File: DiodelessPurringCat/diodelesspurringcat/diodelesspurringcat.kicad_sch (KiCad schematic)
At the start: 21 parts, among them J1 ScreenL, U1 ProMicro-kbd

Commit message: trying to make a reversible nice view
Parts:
- 0/9, 1/8, 10/19, 11/18, 12/17, 13/16, 14/15, 2/7, 20/25, 21/24, 22/23, 26/29, 27/28, 3/6, 4/5: footprint keyswitches:Kailh_socket_PG1350_reversible -> chelming-kbd:choc_v1_hotswap_reversible_no_extras
- J1: value ScreenL -> nice!view; footprint Connector_PinHeader_2.54mm:PinHeader_1x05_P2.54mm_Vertical -> chelming-kbd:nice-view_reversible
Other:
- moved on the sheet: J1
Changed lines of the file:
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@@
 	(polyline
 		(pts
-			(xy 227.33 124.46) (xy 205.74 124.46)
+			(xy 199.39 118.11) (xy 199.39 96.52)
 		)
 		(stroke
@@
 		)
 	)
+	(wire
+		(pts
+			(xy 205.74 111.76) (xy 208.28 111.76)
+		)
+		(stroke
+			(width 0)
+			(type default)
+		)
+	)
+	(wire
+		(pts
+			(xy 207.01 104.14) (xy 215.9 104.14)
+		)
+		(stroke
+			(width 0)
+			(type default)
+		)
+	)
+	(wire
+		(pts
+			(xy 205.74 116.84) (xy 215.9 116.84)
+		)
+		(stroke
+			(width 0)
+			(type default)
+		)
+	)
+	(wire
+		(pts
+			(xy 215.9 97.79) (xy 215.9 101.6)
+		)
+		(stroke
+			(width 0)
+			(type default)
+		)
+	)
+	(wire
+		(pts
+			(xy 215.9 116.84) (xy 215.9 111.76)
+		)
+		(stroke
+			(width 0)
+			(type default)
+		)
+	)
 	(polyline
 		(pts
-			(xy 227.33 90.17) (xy 227.33 124.46)
+			(xy 233.68 118.11) (xy 199.39 118.11)
 		)
 		(stroke
@@
 	(polyline
 		(pts
-			(xy 205.74 124.46) (xy 205.74 90.17)
+			(xy 199.39 96.52) (xy 233.68 96.52)
 		)
 		(stroke
@@
 	(polyline
 		(pts
-			(xy 205.74 90.17) (xy 227.33 90.17)
+			(xy 233.68 96.52) (xy 233.68 118.11)
 		)
 		(stroke
@@
 		)
 	)
+	(wire
+		(pts
+			(xy 208.28 109.22) (xy 215.9 109.22)
+		)
+		(stroke
+			(width 0)
+			(type default)
+		)
+	)
+	(wire
+		(pts
+			(xy 207.01 106.68) (xy 215.9 106.68)
+		)
+		(stroke
+			(width 0)
+			(type default)
+		)
+	)
+	(wire
+		(pts
+			(xy 208.28 111.76) (xy 208.28 109.22)
+		)
+		(stroke
+			(width 0)
+			(type default)
+		)
+	)
 	(polyline
 		(pts
@@
 		)
 	)
+	(wire
+		(pts
+			(xy 207.01 97.79) (xy 215.9 97.79)
+		)
+		(stroke
+			(width 0)
+			(type default)
+		)
+	)
 	(polyline
 		(pts
@@
 	(text "Screen"
 		(exclude_from_sim no)
-		(at 207.01 95.25 0)
+		(at 199.136 95.25 0)
 		(effects
 			(font
@@
 	(global_label "gnd"
 		(shape input)
-		(at 218.44 109.22 270)
-		(fields_autoplaced yes)
-		(effects
-			(font
-				(size 1.27 1.27)
-			)
-			(justify right)
-		)
-		(property "Intersheetrefs" "${INTERSHEET_REFS}"
-			(at 218.3606 114.9913 90)
+		(at 205.74 111.76 180)
+		(fields_autoplaced yes)
+		(effects
+			(font
+				(size 1.27 1.27)
+			)
+			(justify right)
+		)
+		(property "Intersheetrefs" "${INTERSHEET_REFS}"
+			(at 199.962 111.76 0)
 			(effects
 				(font
@@
 	(global_label "CS"
 		(shape input)
-		(at 220.98 109.22 270)
-		(fields_autoplaced yes)
-		(effects
-			(font
-				(size 1.27 1.27)
-			)
-			(justify right)
-		)
-		(property "Intersheetrefs" "${INTERSHEET_REFS}"
-			(at 220.9006 114.0237 90)
+		(at 205.74 116.84 180)
+		(fields_autoplaced yes)
+		(effects
+			(font
+				(size 1.27 1.27)
+			)
+			(justify right)
+		)
+		(property "Intersheetrefs" "${INTERSHEET_REFS}"
+			(at 200.9295 116.84 0)
 			(effects
 				(font
@@
 	(global_label "vcc"
 		(shape input)
-		(at 215.9 109.22 270)
-		(fields_autoplaced yes)
-		(effects
-			(font
-				(size 1.27 1.27)
-			)
-			(justify right)
-		)
-		(property "Intersheetrefs" "${INTERSHEET_REFS}"
-			(at 215.8206 114.689 90)
+		(at 207.01 106.68 180)
+		(fields_autoplaced yes)
+		(effects
+			(font
+				(size 1.27 1.27)
+			)
+			(justify right)
+		)
+		(property "Intersheetrefs" "${INTERSHEET_REFS}"
+			(at 201.5342 106.68 0)
 			(effects
 				(font
@@
 	(global_label "SCK"
 		(shape input)
-		(at 213.36 109.22 270)
-		(fields_autoplaced yes)
-		(effects
-			(font
-				(size 1.27 1.27)
-			)
-			(justify right)
-		)
-		(property "Intersheetrefs" "${INTERSHEET_REFS}"
-			(at 213.2806 115.2937 90)
+		(at 207.01 104.14 180)
+		(fields_autoplaced yes)
+		(effects
+			(font
+				(size 1.27 1.27)
+			)
+			(justify right)
+		)
+		(property "Intersheetrefs" "${INTERSHEET_REFS}"
+			(at 200.9295 104.14 0)
 			(effects
 				(font
@@
 	(global_label "MOSI"
 		(shape input)
-		(at 210.82 109.22 270)
-		(fields_autoplaced yes)
-		(effects
-			(font
-				(size 1.27 1.27)
-			)
-			(justify right)
-		)
-		(property "Intersheetrefs" "${INTERSHEET_REFS}"
-			(at 210.7406 116.1404 90)
+		(at 207.01 97.79 180)
+		(fields_autoplaced yes)
+		(effects
+			(font
+				(size 1.27 1.27)
+			)
+			(justify right)
+		)
+		(property "Intersheetrefs" "${INTERSHEET_REFS}"
+			(at 200.0828 97.79 0)
 			(effects
 				(font
@@
 			)
 		)
-		(property "Footprint" "keyswitches:Kailh_socket_PG1350_reversible"
+		(property "Footprint" "chelming-kbd:choc_v1_hotswap_reversible_no_extras"
 			(at 26.67 33.02 0)
 			(effects
@@
 			)
 		)
-		(property "Footprint" "keyswitches:Kailh_socket_PG1350_reversible"
+		(property "Footprint" "chelming-kbd:choc_v1_hotswap_reversible_no_extras"
 			(at 49.53 24.13 0)
 			(effects
@@
 			)
 		)
-		(property "Footprint" "keyswitches:Kailh_socket_PG1350_reversible"
+		(property "Footprint" "chelming-kbd:choc_v1_hotswap_reversible_no_extras"
 			(at 72.39 20.32 0)
 			(effects
@@
 			)
 		)
-		(property "Footprint" "keyswitches:Kailh_socket_PG1350_reversible"
+		(property "Footprint" "chelming-kbd:choc_v1_hotswap_reversible_no_extras"
 			(at 95.25 24.13 0)
 			(effects
@@
 			)
 		)
-		(property "Footprint" "keyswitches:Kailh_socket_PG1350_reversible"
+		(property "Footprint" "chelming-kbd:choc_v1_hotswap_reversible_no_extras"
 			(at 95.25 86.36 0)
 			(effects
@@
 			)
 		)
-		(property "Footprint" "keyswitches:Kailh_socket_PG1350_reversible"
+		(property "Footprint" "chelming-kbd:choc_v1_hotswap_reversible_no_extras"
 			(at 26.67 54.61 0)
 			(effects
@@
 			)
 		)
-		(property "Footprint" "keyswitches:Kailh_socket_PG1350_reversible"
+		(property "Footprint" "chelming-kbd:choc_v1_hotswap_reversible_no_extras"
 			(at 49.53 45.72 0)
 			(effects
@@
 			)
 		)
-		(property "Footprint" "keyswitches:Kailh_socket_PG1350_reversible"
+		(property "Footprint" "chelming-kbd:choc_v1_hotswap_reversible_no_extras"
 			(at 72.39 41.91 0)
 			(effects
@@
 			)
 		)
-		(property "Footprint" "keyswitches:Kailh_socket_PG1350_reversible"
+		(property "Footprint" "chelming-kbd:choc_v1_hotswap_reversible_no_extras"
 			(at 95.25 45.72 0)
 			(effects
@@
 			)
 		)
-		(property "Footprint" "keyswitches:Kailh_socket_PG1350_reversible"
+		(property "Footprint" "chelming-kbd:choc_v1_hotswap_reversible_no_extras"
 			(at 49.53 64.77 0)
 			(effects
@@
 			)
 		)
-		(property "Footprint" "keyswitches:Kailh_socket_PG1350_reversible"
+		(property "Footprint" "chelming-kbd:choc_v1_hotswap_reversible_no_extras"
 			(at 72.39 60.96 0)
 			(effects
@@
 			)
 		)
-		(property "Footprint" "keyswitches:Kailh_socket_PG1350_reversible"
+		(property "Footprint" "chelming-kbd:choc_v1_hotswap_reversible_no_extras"
 			(at 95.25 64.77 0)
 			(effects
@@
 			)
 		)
-		(property "Footprint" "keyswitches:Kailh_socket_PG1350_reversible"
+		(property "Footprint" "chelming-kbd:choc_v1_hotswap_reversible_no_extras"
 			(at 118.11 34.29 0)
 			(effects
@@
 			)
 		)
-		(property "Footprint" "keyswitches:Kailh_socket_PG1350_reversible"
+		(property "Footprint" "chelming-kbd:choc_v1_hotswap_reversible_no_extras"
 			(at 118.11 55.88 0)
 			(effects
@@
 	(symbol
 		(lib_id "Connector_Generic:Conn_01x05")
-		(at 215.9 104.14 90)
+		(at 220.98 106.68 0)
 		(unit 1)
 		(exclude_from_sim no)
@@
 		(fields_autoplaced yes)
 		(property "Reference" "J1"
-			(at 215.9 97.79 90)
-			(effects
-				(font
-					(size 1.27 1.27)
-				)
-			)
-		)
-		(property "Value" "ScreenL"
-			(at 215.9 100.33 90)
-			(effects
-				(font
-					(size 1.27 1.27)
-				)
-			)
-		)
-		(property "Footprint" "Connector_PinHeader_2.54mm:PinHeader_1x05_P2.54mm_Vertical"
-			(at 215.9 104.14 0)
+			(at 227.33 106.68 90)
+			(effects
+				(font
+					(size 1.27 1.27)
+				)
+			)
+		)
+		(property "Value" "nice!view"
+			(at 224.79 106.68 90)
+			(effects
+				(font
+					(size 1.27 1.27)
+				)
+			)
+		)
+		(property "Footprint" "chelming-kbd:nice-view_reversible"
+			(at 220.98 106.68 0)
 			(effects
 				(font
@@
 		)
 		(property "Datasheet" "~"
-			(at 215.9 104.14 0)
+			(at 220.98 106.68 0)
 			(effects
 				(font
@@
 		)
 		(property "Description" ""
-			(at 215.9 104.14 0)
+			(at 220.98 106.68 0)
 			(effects
 				(font
@@
 			)
 		)
-		(property "Footprint" "keyswitches:Kailh_socket_PG1350_reversible"
+		(property "Footprint" "chelming-kbd:choc_v1_hotswap_reversible_no_extras"
 			(at 118.11 86.36 0)
 			(effects

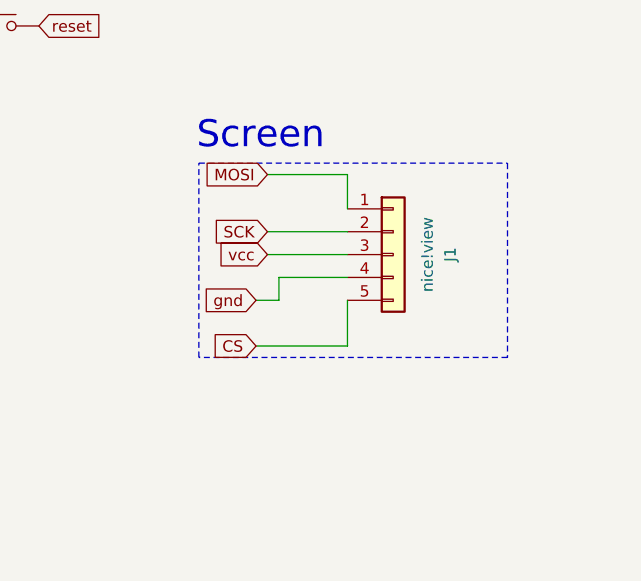
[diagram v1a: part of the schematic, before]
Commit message: moving back to reversible. still diodeless. needs case mounts
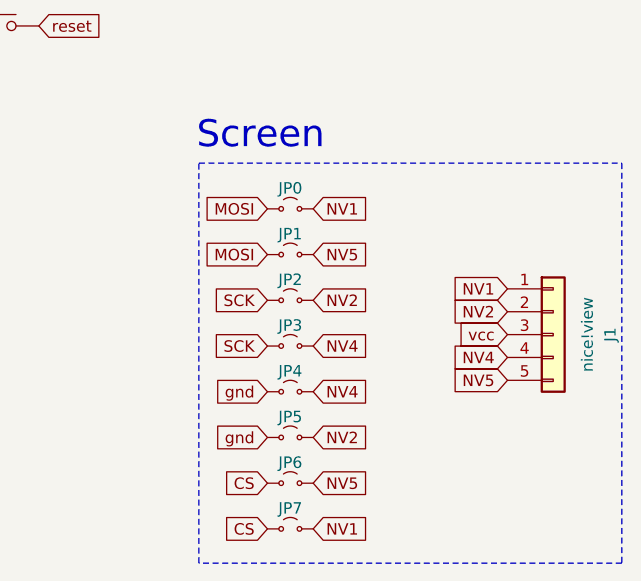
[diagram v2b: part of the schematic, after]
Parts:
- added JP0, JP1, JP2, JP3, JP4, JP5, JP6, JP7: Jumper_2_Small_Open, Jumper:SolderJumper-2_P1.3mm_Open_TrianglePad1.0x1.5mm, symbol Jumper:Jumper_2_Small_Open
- J1: footprint chelming-kbd:nice-view_reversible -> nice_view:nice_view
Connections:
- net CS: now also JP6.1 (A), JP7.1 (A); no longer J1.5 (Pin_5)
- net MOSI: now also JP0.1 (A), JP1.1 (A); no longer J1.1 (Pin_1)
- net SCK: now also JP2.1 (A), JP3.1 (A); no longer J1.2 (Pin_2)
- net gnd: now also JP4.1 (A), JP5.1 (A); no longer J1.4 (Pin_4)
- new net NV1: J1.1 (Pin_1), JP0.2 (B), JP7.2 (B)
- new net NV2: J1.2 (Pin_2), JP2.2 (B), JP5.2 (B)
- new net NV4: J1.4 (Pin_4), JP3.2 (B), JP4.2 (B)
- new net NV5: J1.5 (Pin_5), JP1.2 (B), JP6.2 (B)
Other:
- moved on the sheet: J1
